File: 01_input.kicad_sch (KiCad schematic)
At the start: 24 parts, among them J3 Conn_01x04, U2 VOS618A, U3 LMR51406YDBV

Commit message: Schematic: Update, annotate
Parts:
- removed J3: Conn_01x04, Connector_Molex:Molex_PicoBlade_53398-0471_1x04-1MP_P1.25mm_Vertical, symbol Connector_Generic:Conn_01x04
- removed JP1: ~, Jumper:SolderJumper-2_P1.3mm_Bridged_RoundedPad1.0x1.5mm, symbol Jumper:SolderJumper_2_Bridged
- added C8: 100n, Capacitor_SMD:C_0402_1005Metric, symbol Device:C
- added FB1: BLM15PX601SZ1D, Inductor_SMD:L_0402_1005Metric, symbol Device:FerriteBead_Small
- added J1: 0533980471, Connector_Molex:Molex_PicoBlade_53398-0471_1x04-1MP_P1.25mm_Vertical, symbol Connector_Generic_MountingPin:Conn_01x04_MountingPin
- added TP2, TP3: ~, TestPoint:TestPoint_Pad_D1.0mm, symbol Connector:TestPoint
- renumbered C7 to C1, C6 to C2, C11 to C3, C10 to C4, C3 to C5, C4 to C6, C5 to C7, C14 to C9, D9 to D1, D10 to D2, D11 to D3, JP2 to JP1, L2 to L1, R8 to R1, R6 to R2, R1 to R3, R2 to R4, TP3 to TP1, TP2 to TP4, U2 to U1, U3 to U2
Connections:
- net 3V3: now also C8.1, FB1.2, TP2.1
- net GND: now also C8.2, J1.2 (Pin_2), J1.MP (MountPin), TP3.1
- net at C4.2, D3.2 (A), U1.2: now also J1.4 (Pin_4)
- net at C3.1, R2.2: now also J1.3 (Pin_3)
- net at C9.2, L1.2, R3.1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: now also FB1.1
- net at F1.1: now also J1.1 (Pin_1)
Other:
- moved on the sheet: C5, C6, C7, C9, JP1, L1, R3, R4, TP4, U2

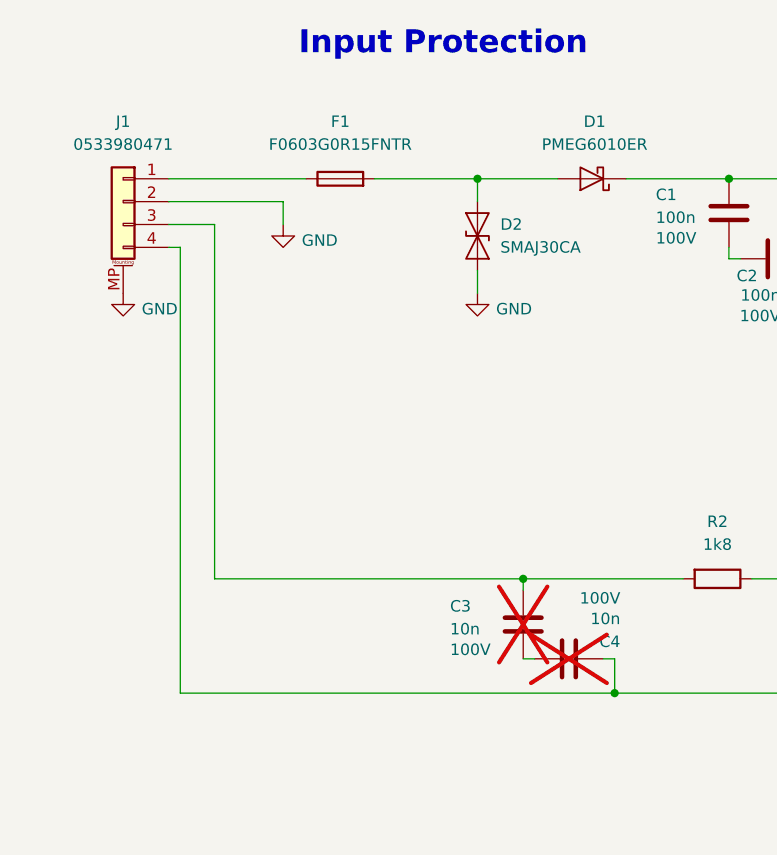
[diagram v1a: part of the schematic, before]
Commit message: Schematic: Adjust pinouts for easier routing
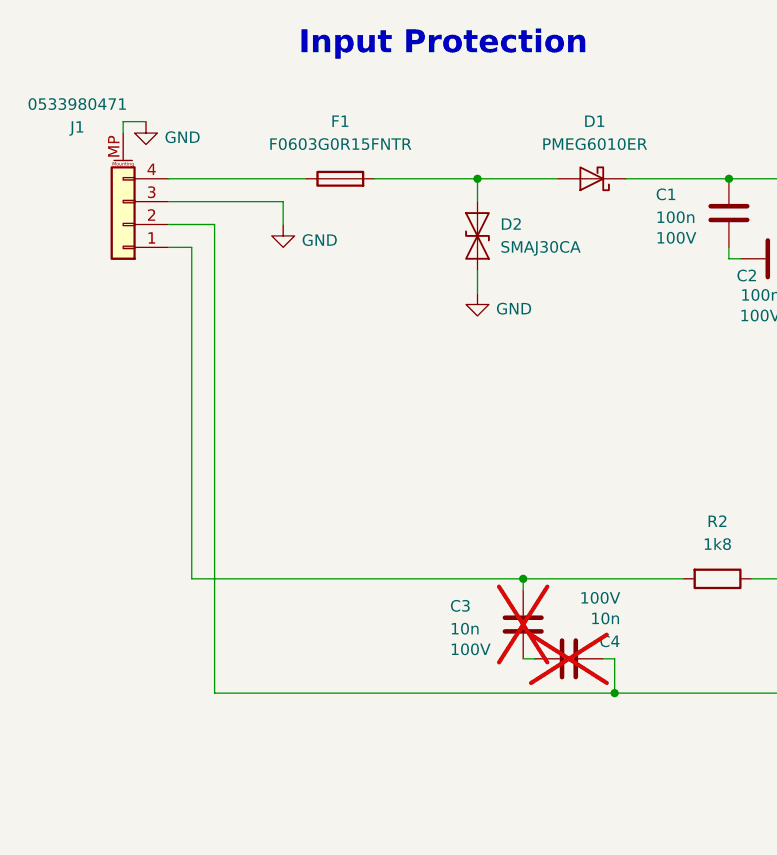
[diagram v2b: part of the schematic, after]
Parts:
- C5, C7: footprint Capacitor_SMD:C_0603_1608Metric -> Capacitor_SMD:C_0402_1005Metric
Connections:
- net GND: now also J1.3 (Pin_3); no longer J1.2 (Pin_2)
- net at C4.2, D3.2 (A), U1.2: now also J1.2 (Pin_2); no longer J1.4 (Pin_4)
- net at J1.1 (Pin_1): now also C3.1, R2.2; no longer F1.1
- new net: F1.1, J1.4 (Pin_4)
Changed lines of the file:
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@@
 	(wire
 		(pts
-			(xy 46.99 41.91) (xy 46.99 91.44)
+			(xy 50.8 39.37) (xy 50.8 91.44)
 		)
 		(stroke
@@
 	(wire
 		(pts
-			(xy 50.8 39.37) (xy 45.72 39.37)
-		)
-		(stroke
-			(width 0)
-			(type default)
-		)
-	)
-	(wire
-		(pts
 			(xy 118.11 91.44) (xy 143.51 91.44)
 		)
@@
 	(wire
 		(pts
-			(xy 50.8 78.74) (xy 50.8 39.37)
+			(xy 147.32 87.63) (xy 143.51 87.63)
 		)
 		(stroke
@@
 	(wire
 		(pts
-			(xy 147.32 87.63) (xy 143.51 87.63)
+			(xy 80.01 34.29) (xy 80.01 36.83)
 		)
 		(stroke
@@
 	(wire
 		(pts
-			(xy 80.01 34.29) (xy 80.01 36.83)
+			(xy 40.64 29.21) (xy 40.64 27.94)
 		)
 		(stroke
@@
 	(wire
 		(pts
+			(xy 40.64 27.94) (xy 43.18 27.94)
+		)
+		(stroke
+			(width 0)
+			(type default)
+		)
+	)
+	(wire
+		(pts
 			(xy 143.51 87.63) (xy 143.51 91.44)
 		)
@@
 	(wire
 		(pts
-			(xy 50.8 78.74) (xy 85.09 78.74)
+			(xy 48.26 78.74) (xy 85.09 78.74)
 		)
 		(stroke
@@
 	(wire
 		(pts
+			(xy 50.8 39.37) (xy 45.72 39.37)
+		)
+		(stroke
+			(width 0)
+			(type default)
+		)
+	)
+	(wire
+		(pts
 			(xy 104.14 151.13) (xy 100.33 151.13)
 		)
@@
 	(wire
 		(pts
+			(xy 45.72 41.91) (xy 48.26 41.91)
+		)
+		(stroke
+			(width 0)
+			(type default)
+		)
+	)
+	(wire
+		(pts
 			(xy 118.11 78.74) (xy 118.11 81.28)
 		)
@@
 	(wire
 		(pts
+			(xy 48.26 41.91) (xy 48.26 78.74)
+		)
+		(stroke
+			(width 0)
+			(type default)
+		)
+	)
+	(wire
+		(pts
 			(xy 96.52 34.29) (xy 107.95 34.29)
 		)
@@
 	(wire
 		(pts
-			(xy 46.99 91.44) (xy 95.25 91.44)
+			(xy 50.8 91.44) (xy 95.25 91.44)
 		)
 		(stroke
@@
 		)
 	)
-	(wire
-		(pts
-			(xy 46.99 41.91) (xy 45.72 41.91)
-		)
-		(stroke
-			(width 0)
-			(type default)
-		)
-	)
 	(text "Input Protection"
 		(exclude_from_sim no)
@@
 	)
 	(symbol
+		(lib_id "Connector_Generic_MountingPin:Conn_01x04_MountingPin")
+		(at 40.64 39.37 180)
+		(unit 1)
+		(exclude_from_sim no)
+		(in_bom yes)
+		(on_board yes)
+		(dnp no)
+		(property "Reference" "J1"
+			(at 35.56 28.575 0)
+			(effects
+				(font
+					(size 1.27 1.27)
+				)
+			)
+		)
+		(property "Value" "0533980471"
+			(at 35.56 26.035 0)
+			(effects
+				(font
+					(size 1.27 1.27)
+				)
+			)
+		)
+		(property "Footprint" "Connector_Molex:Molex_PicoBlade_53398-0471_1x04-1MP_P1.25mm_Vertical"
+			(at 40.64 39.37 0)
+			(effects
+				(font
+					(size 1.27 1.27)
+				)
+				(hide yes)
+			)
+		)
+		(property "Datasheet" "~"
+			(at 40.64 39.37 0)
+			(effects
+				(font
+					(size 1.27 1.27)
+				)
+				(hide yes)
+			)
+		)
+		(property "Description" ""
+			(at 40.64 39.37 0)
+			(effects
+				(font
+					(size 1.27 1.27)
+				)
+				(hide yes)
+			)
+		)
+		(property "MPN" ""
+			(at 40.64 39.37 0)
+			(effects
+				(font
+					(size 1.27 1.27)
+				)
+				(hide yes)
+			)
+		)
+		(property "No_BOM" ""
+			(at 40.64 39.37 0)
+			(effects
+				(font
+					(size 1.27 1.27)
+				)
+				(hide yes)
+			)
+		)
+		(pin "MP"
+		)
+		(pin "3"
+		)
+		(pin "4"
+		)
+		(pin "2"
+		)
+		(pin "1"
+		)
+		(instances
+			(project "ShiftLight"
+				(path "/db7756aa-b7f6-4357-ad6e-f204384e9cf5/c0066c6c-44dc-49da-889b-b666c4212450"
+					(reference "J1")
+					(unit 1)
+				)
+			)
+		)
+	)
+	(symbol
 		(lib_id "power:GND")
 		(at 63.5 149.86 0)
@@
 			)
 		)
-		(property "Footprint" "Capacitor_SMD:C_0603_1608Metric"
+		(property "Footprint" "Capacitor_SMD:C_0402_1005Metric"
 			(at 69.5452 148.59 0)
 			(effects
@@
 	)
 	(symbol
-		(lib_id "Connector_Generic_MountingPin:Conn_01x04_MountingPin")
-		(at 40.64 36.83 0)
-		(mirror y)
-		(unit 1)
-		(exclude_from_sim no)
-		(in_bom yes)
-		(on_board yes)
-		(dnp no)
-		(fields_autoplaced yes)
-		(property "Reference" "J1"
-			(at 40.64 27.94 0)
-			(effects
-				(font
-					(size 1.27 1.27)
-				)
-			)
-		)
-		(property "Value" "0533980471"
-			(at 40.64 30.48 0)
-			(effects
-				(font
-					(size 1.27 1.27)
-				)
-			)
-		)
-		(property "Footprint" "Connector_Molex:Molex_PicoBlade_53398-0471_1x04-1MP_P1.25mm_Vertical"
-			(at 40.64 36.83 0)
-			(effects
-				(font
-					(size 1.27 1.27)
-				)
-				(hide yes)
-			)
-		)
-		(property "Datasheet" "~"
-			(at 40.64 36.83 0)
-			(effects
-				(font
-					(size 1.27 1.27)
-				)
-				(hide yes)
-			)
-		)
-		(property "Description" ""
-			(at 40.64 36.83 0)
-			(effects
-				(font
-					(size 1.27 1.27)
-				)
-				(hide yes)
-			)
-		)
-		(property "MPN" ""
-			(at 40.64 36.83 0)
-			(effects
-				(font
-					(size 1.27 1.27)
-				)
-				(hide yes)
-			)
-		)
-		(property "No_BOM" ""
-			(at 40.64 36.83 0)
-			(effects
-				(font
-					(size 1.27 1.27)
-				)
-				(hide yes)
-			)
-		)
-		(pin "MP"
-		)
-		(pin "3"
-		)
-		(pin "4"
-		)
-		(pin "2"
-		)
-		(pin "1"
-		)
-		(instances
-			(project ""
-				(path "/db7756aa-b7f6-4357-ad6e-f204384e9cf5/c0066c6c-44dc-49da-889b-b666c4212450"
-					(reference "J1")
-					(unit 1)
-				)
-			)
-		)
-	)
-	(symbol
 		(lib_id "power:GND")
 		(at 160.02 157.48 0)
@@
 			)
 		)
-		(property "Footprint" "Capacitor_SMD:C_0603_1608Metric"
+		(property "Footprint" "Capacitor_SMD:C_0402_1005Metric"
 			(at 103.8352 147.32 0)
 			(effects
@@
 	(symbol
 		(lib_id "power:GND")
-		(at 40.64 46.99 0)
+		(at 43.18 27.94 0)
 		(unit 1)
 		(exclude_from_sim no)
@@
 		(dnp no)
 		(property "Reference" "#PWR04"
-			(at 40.64 53.34 0)
+			(at 43.18 34.29 0)
 			(effects
 				(font
@@
 		)
 		(property "Value" "GND"
-			(at 44.704 48.768 0)
+			(at 47.244 29.718 0)
 			(effects
 				(font
@@
 		)
 		(property "Footprint" ""
-			(at 40.64 46.99 0)
+			(at 43.18 27.94 0)
 			(effects
 				(font
@@
 		)
 		(property "Datasheet" ""
-			(at 40.64 46.99 0)
+			(at 43.18 27.94 0)
 			(effects
 				(font
@@
 		)
 		(property "Description" "Power symbol creates a global label with name \"GND\" , ground"
-			(at 40.64 46.99 0)
+			(at 43.18 27.94 0)
 			(effects
 				(font
@@
 		)
 		(property "MPN" ""
-			(at 40.64 46.99 0)
+			(at 43.18 27.94 0)
 			(effects
 				(font
@@
 		)
 		(property "No_BOM" ""
-			(at 40.64 46.99 0)
+			(at 43.18 27.94 0)
 			(effects
 				(font

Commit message: Add personal library
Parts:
- D3: symbol Personal_lib:VESD05B1-02V -> Personal_Lib:VESD05B1-02V
- L1: footprint Inductor_SMD:L_TDK_VLS3015CX -> Personal_Lib:L_TDK_VLS3015CX; symbol Personal_lib:L_WindingIndicator -> Personal_Lib:L_WindingIndicator
- U2: symbol Personal_lib:LMR51406YDBV -> Personal_Lib:LMR51406YDBV
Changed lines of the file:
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@@
 	)
 	(symbol
-		(lib_id "Personal_lib:LMR51406YDBV")
+		(lib_id "Personal_Lib:LMR51406YDBV")
 		(at 90.17 142.24 0)
 		(unit 1)
@@
 	)
 	(symbol
-		(lib_id "Personal_lib:L_WindingIndicator")
+		(lib_id "Personal_Lib:L_WindingIndicator")
 		(at 113.03 147.32 90)
 		(unit 1)
@@
 			)
 		)
-		(property "Footprint" "Inductor_SMD:L_TDK_VLS3015CX"
+		(property "Footprint" "Personal_Lib:L_TDK_VLS3015CX"
 			(at 113.03 147.32 0)
 			(effects
@@
 	)
 	(symbol
-		(lib_id "Personal_lib:VESD05B1-02V")
+		(lib_id "Personal_Lib:VESD05B1-02V")
 		(at 118.11 85.09 270)
 		(unit 1)

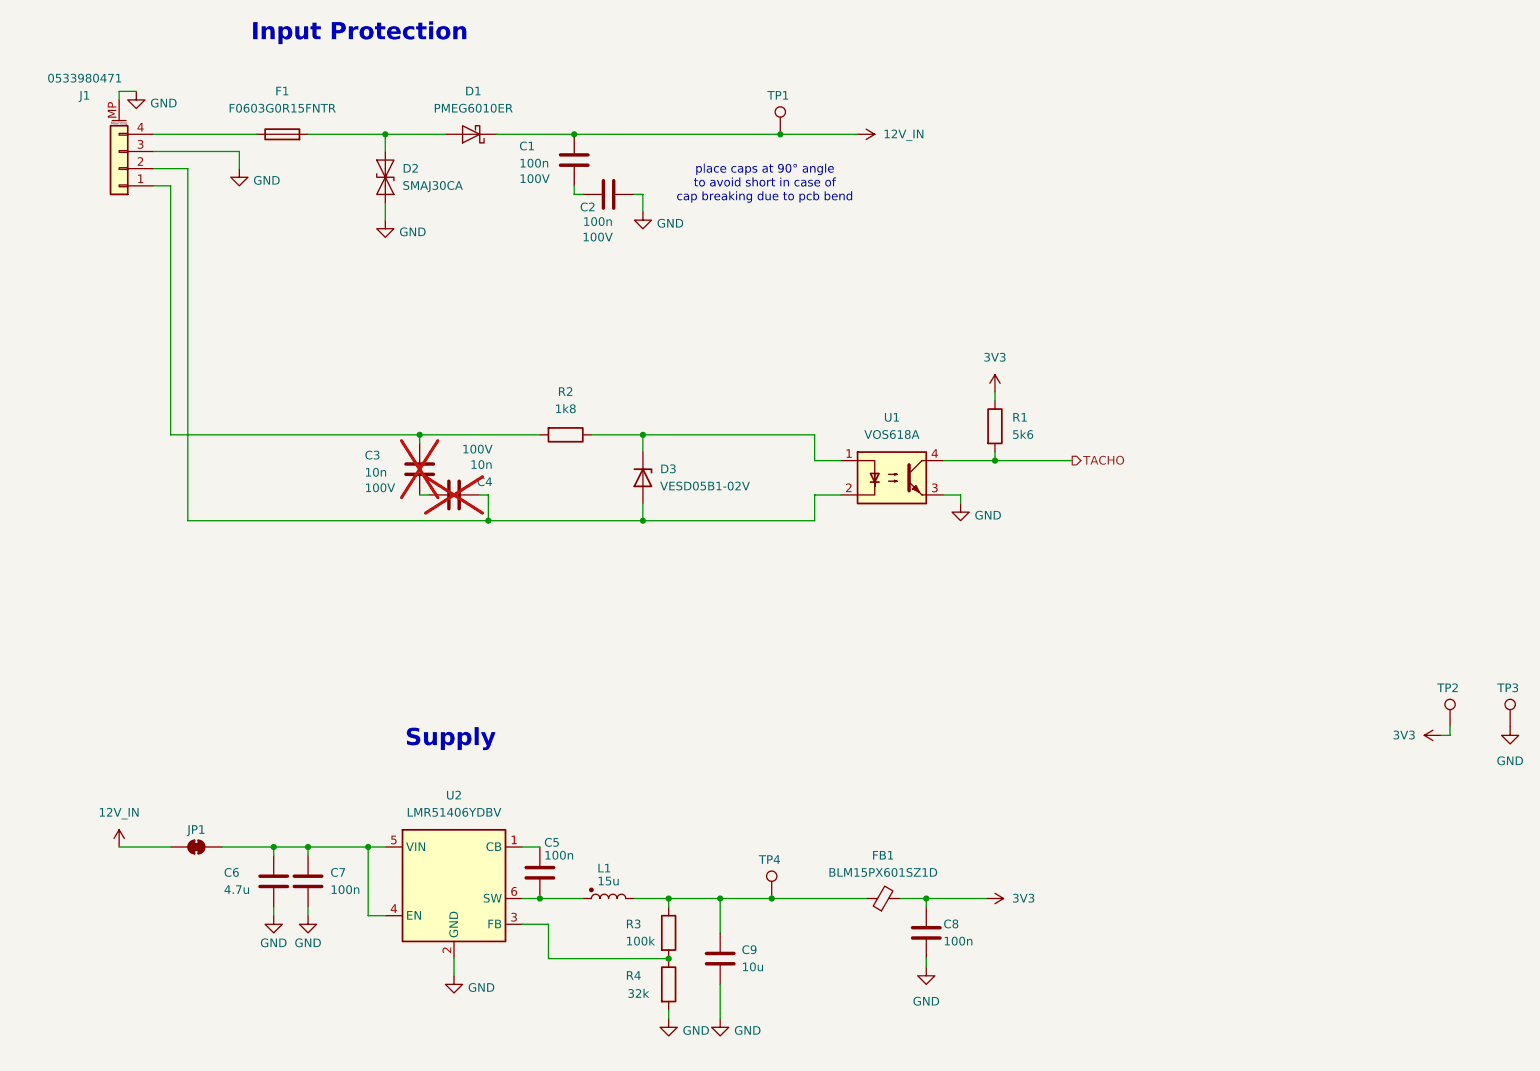
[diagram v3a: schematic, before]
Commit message: Schematic: Add PWR_FLAGs to fix ERC errors
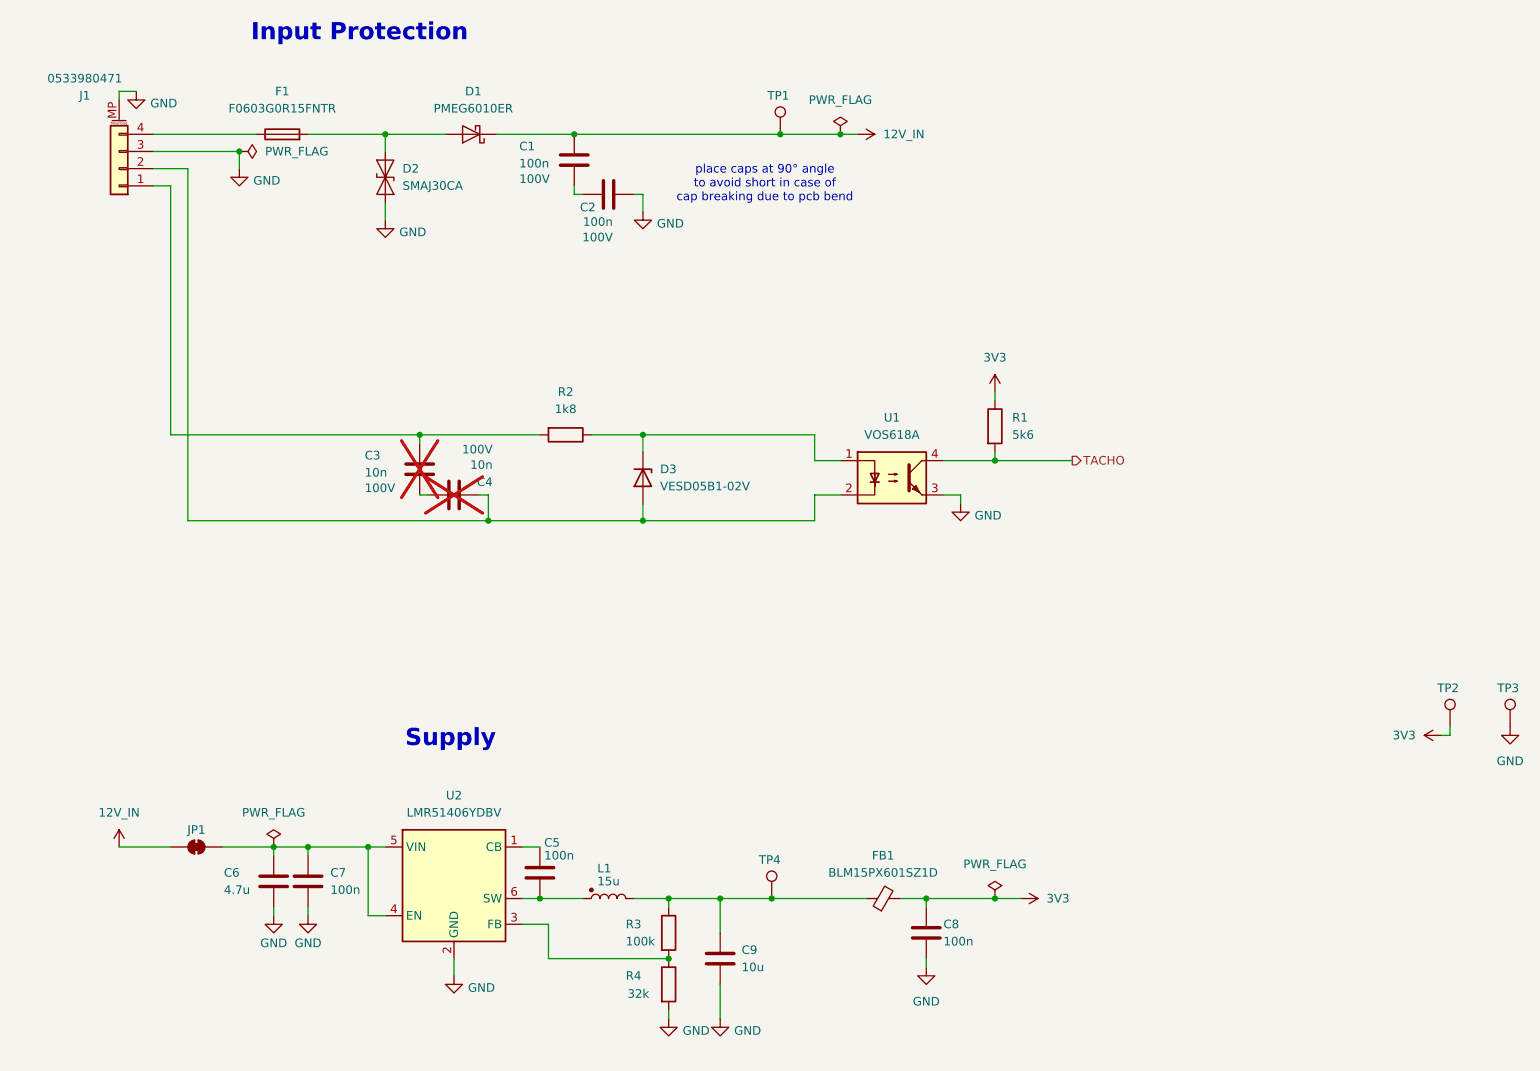
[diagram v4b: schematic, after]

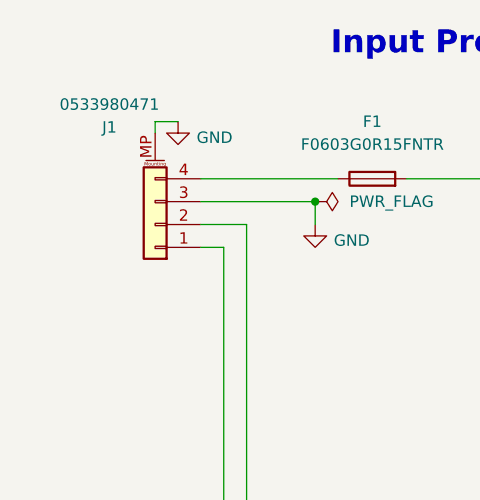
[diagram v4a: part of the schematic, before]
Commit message: Schematic: Remove nRST net label to avoid ERC warning
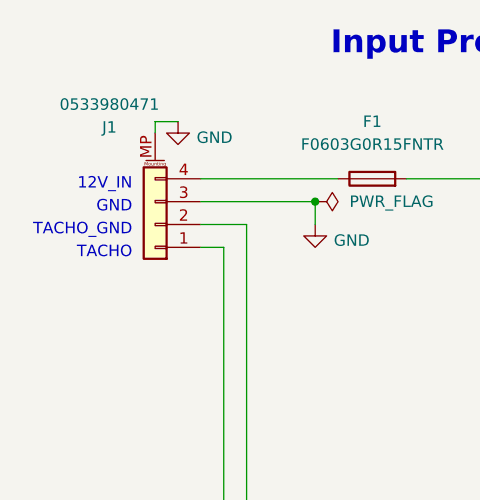
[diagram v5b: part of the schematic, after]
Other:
- note added: "12V_IN"
- note added: "GND"
- note added: "TACHO"
- note added: "TACHO_GND"
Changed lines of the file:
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@@
+		)
+	)
+	(text "TACHO"
+		(exclude_from_sim no)
+		(at 38.1 42.545 0)
+		(effects
+			(font
+				(size 1.27 1.27)
+			)
+			(justify right)
 		)
 	)
@@
 		)
 	)
+	(text "12V_IN"
+		(exclude_from_sim no)
+		(at 38.1 34.925 0)
+		(effects
+			(font
+				(size 1.27 1.27)
+			)
+			(justify right)
+		)
+	)
+	(text "GND"
+		(exclude_from_sim no)
+		(at 38.1 37.465 0)
+		(effects
+			(font
+				(size 1.27 1.27)
+			)
+			(justify right)
+		)
+	)
+	(text "TACHO_GND"
+		(exclude_from_sim no)
+		(at 38.1 40.005 0)
+		(effects
+			(font
+				(size 1.27 1.27)
+			)
+			(justify right)
+		)
+	)

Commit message: Ci: Fill title header in generated schematic
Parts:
- JP1: No_BOM (none) -> YES
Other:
- title: (none) -> ${PROJECTNAME}
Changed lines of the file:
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@@
 	(generator_version "8.0")
 	(paper "A4")
+	(title_block
+		(title "${PROJECTNAME}")
+		(date "${ISSUE_DATE}")
+		(rev "${REVISION}")
+	)
 	(junction
 		(at 80.01 34.29)
@@
 			)
 		)
-		(property "No_BOM" ""
+		(property "No_BOM" "YES"
 			(at 52.07 139.7 0)
 			(effects

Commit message: Schematic: Remove Testpoints from BOM
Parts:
- TP1, TP2, TP3, TP4: now left out of the parts list
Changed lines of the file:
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@@
 		(unit 1)
 		(exclude_from_sim no)
-		(in_bom yes)
+		(in_bom no)
 		(on_board yes)
 		(dnp no)
@@
 		(unit 1)
 		(exclude_from_sim no)
-		(in_bom yes)
+		(in_bom no)
 		(on_board yes)
 		(dnp no)
@@
 		(unit 1)
 		(exclude_from_sim no)
-		(in_bom yes)
+		(in_bom no)
 		(on_board yes)
 		(dnp no)
@@
 		(unit 1)
 		(exclude_from_sim no)
-		(in_bom yes)
+		(in_bom no)
 		(on_board yes)
 		(dnp no)
